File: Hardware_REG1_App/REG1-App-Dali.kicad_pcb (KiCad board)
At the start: 2 copper layers, 83 x 32.8 mm, 27 parts, among them J1 REG1_App_Connector, J3 DALI, Q1 BSS123, Q2 BC857, U1 EL357N(A)(TA)-G, U2 EL357N(A)(TA)-G, U3 STN93003, U4 STN1HNK60

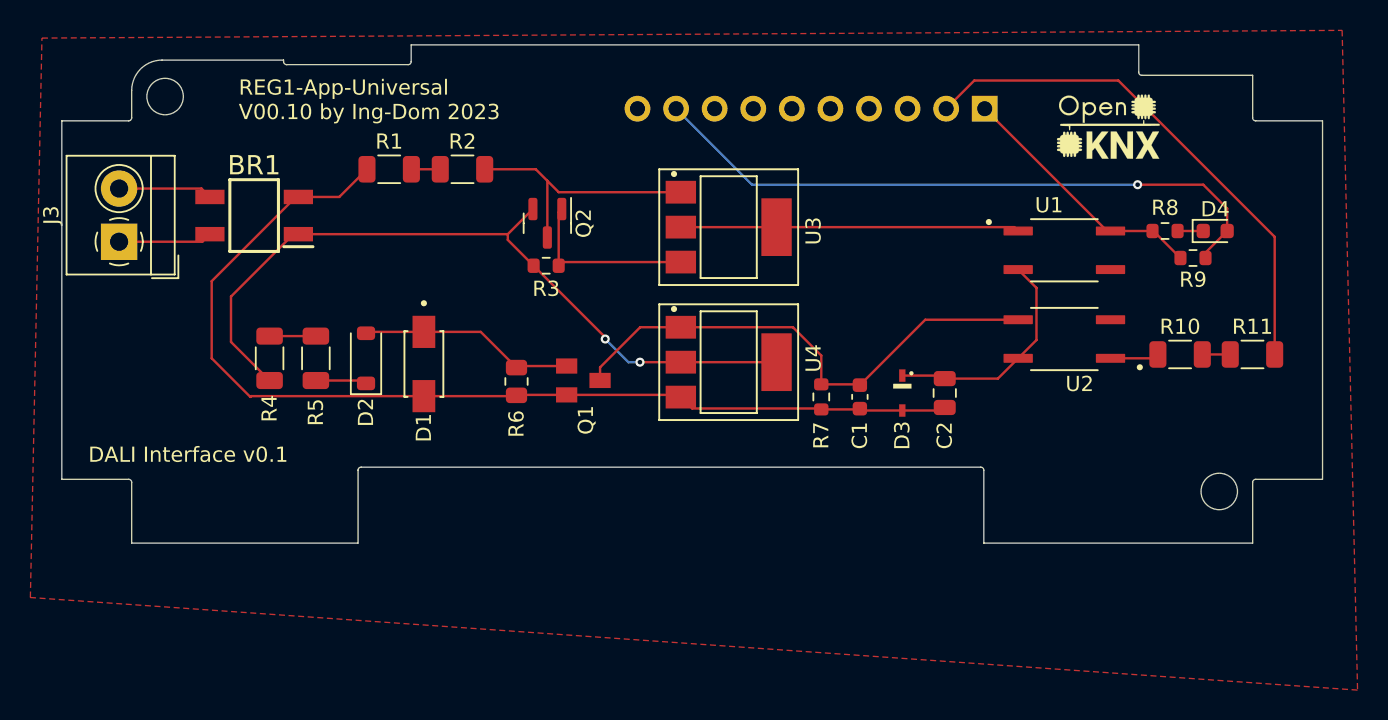
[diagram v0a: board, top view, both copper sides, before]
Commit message: updated REG1 and renamed
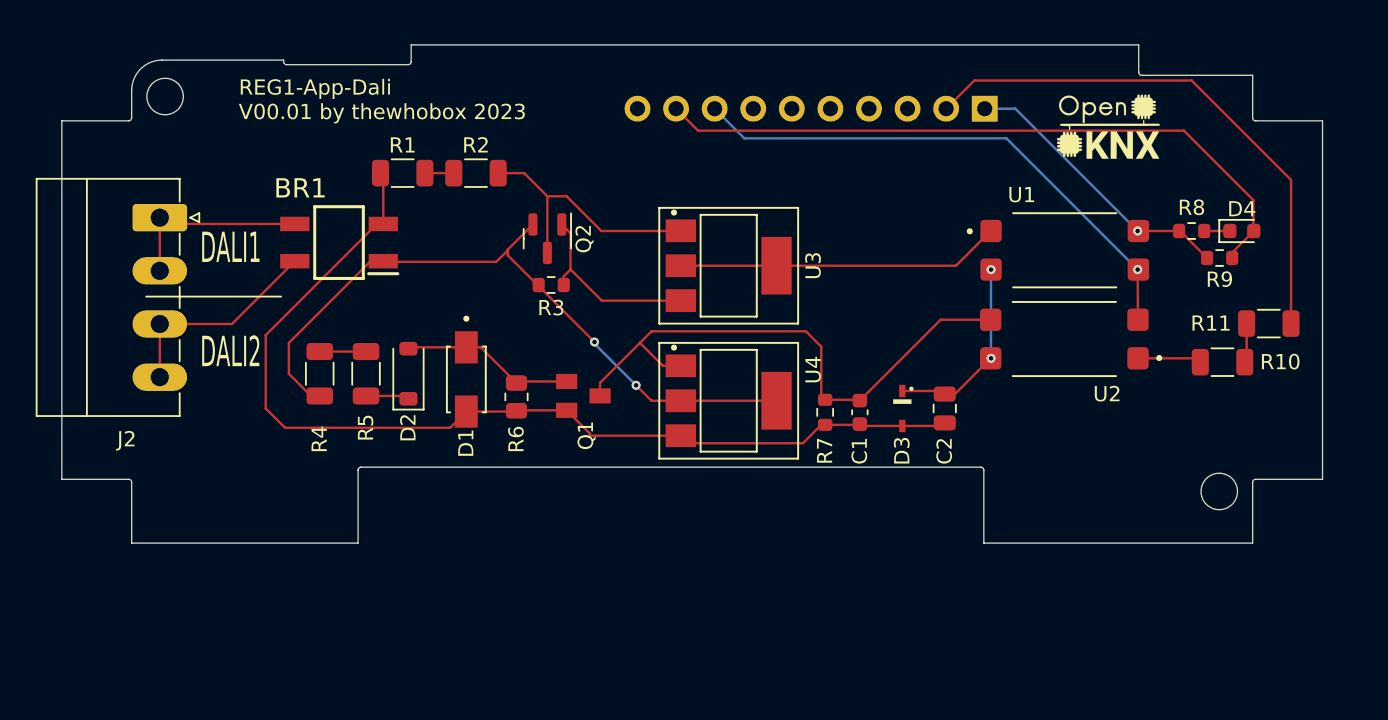
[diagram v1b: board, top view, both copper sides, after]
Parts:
- removed J3: DALI, TerminalBlock_4Ucon:TerminalBlock_4Ucon_1x02_P3.50mm_Horizontal
- added J2: Dali, Connector_Phoenix_MC:PhoenixContact_MC_1,5_4-G-3.5_1x04_P3.50mm_Horizontal, F.Cu at (76.5, 101.5)
- U1, U2: value EL357N(A)(TA)-G -> EL817S1(C)(TU)-F; footprint DALI:SOP254P700X200-4N -> DALI:SOIC254P1030X390-4N
- moved BR1 5.86 mm to (88.2, 103.1)
- moved R4 3.45 mm to (87.0, 111.8)
- moved R5 3.45 mm to (90.0, 111.8)
- moved D1 2.97 mm to (96.6, 112.1)
- moved D2 2.97 mm to (92.8, 111.8)
- moved R10 2.84 mm to (146.4, 111.0)
- moved U3 2.54 mm to (113.9, 104.6)
- moved U4 2.54 mm to (113.9, 113.5)
- moved R11 2.30 mm to (149.5, 108.4)
- moved D4 1.75 mm to (147.7, 102.4)
- moved R8 1.75 mm to (144.4, 102.4)
- moved R9 1.75 mm to (146.2, 104.1)
- moved R3 1.31 mm to (102.2, 105.9)
- moved R7 1.05 mm to (120.3, 114.3)
- moved C1 1.02 mm to (122.5, 114.3)
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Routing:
- net GND: track 0.00 -> 35.6 mm, vias 0 -> 1
- net Net-(BR1-~_2): track 6.18 -> 13.5 mm
- net Net-(BR1-~_1): track 6.21 -> 12.6 mm
- net Dali+: track 50.3 -> 45.5 mm
- net Net-(C1-Pad1): track 34.0 -> 37.4 mm
- net Net-(D2-A): track 14.3 -> 11.5 mm
- net Net-(C2-Pad1): track 15.1 -> 12.7 mm, vias 0 -> 2
- net +3.3V: track 42.8 -> 44.9 mm, vias 1 -> 0
- net DALI-: track 68.3 -> 66.5 mm
- net /D_RX: track 17.0 -> 18.7 mm, vias 0 -> 1
- net /D_TX: track 34.4 -> 35.6 mm
- net Net-(R10-Pad1): track 3.22 -> 4.21 mm
- net Net-(U1-Pad1): track 22.3 -> 21.3 mm
- net Net-(R10-Pad2): track 1.84 -> 2.59 mm
- net Net-(Q2-B): track 12.0 -> 12.5 mm
- removed copper zone on F.Cu, net GND
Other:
- board text added: "DALI1"
- board text added: "DALI2"
- board text added: "REG1-App-Dali V00.01 by thewhobox 2023"
- board text removed: "DALI Interface v0.1"
- board text removed: "REG1-App-Universal V00.10 by Ing-Dom 2023"

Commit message: updated pcb
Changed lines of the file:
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@@
     (pad "4" smd roundrect (at 4.85 -1.27 180) (size 1.41 1.47) (layers "F.Cu" "F.Paste" "F.Mask") (roundrect_rratio 0.18)
       (net 16 "/D_RX") (pintype "passive"))
+    (model "${DALI_3D}/EL817S1_C__TU_.step"
+      (offset (xyz 0 0 0))
+      (scale (xyz 1 1 1))
+      (rotate (xyz -90 0 0))
+    )
   )
   (footprint "DALI:SOT230P700X180-4N" (layer "F.Cu")
@@
     (pad "4" smd rect (at 0 -3.15 90) (size 3.8 2) (layers "F.Cu" "F.Paste" "F.Mask")
       (net 24 "Net-(U1-Pad1)") (pintype "passive"))
+    (model "${DALI_3D}/STN93003.step"
+      (offset (xyz 0 0 0))
+      (scale (xyz 1 1 1))
+      (rotate (xyz -90 0 -90))
+    )
   )
   (footprint "DALI:SOIC254P1030X390-4N" (layer "F.Cu")
@@
     (pad "4" smd roundrect (at 4.85 -1.27) (size 1.41 1.47) (layers "F.Cu" "F.Paste" "F.Mask") (roundrect_rratio 0.18)
       (net 9 "Net-(C2-Pad1)") (pintype "passive"))
+    (model "${DALI_3D}/EL817S1_C__TU_.step"
+      (offset (xyz 0 0 0))
+      (scale (xyz 1 1 1))
+      (rotate (xyz -90 0 0))
+    )
   )
   (footprint "Capacitor_SMD:C_0805_2012Metric" (layer "F.Cu")
@@
     (pad "C" smd rect (at -2.115 0 270) (size 2.12 1.5) (layers "F.Cu" "F.Paste" "F.Mask")
       (net 13 "Net-(D2-A)") (pintype "passive"))
+    (model "${DALI_3D}/1SMA4746.step"
+      (offset (xyz 0 0 0))
+      (scale (xyz 1 1 1))
+      (rotate (xyz -90 0 0))
+    )
   )
   (footprint "Resistor_SMD:R_1206_3216Metric" (layer "F.Cu")
@@
     (fp_line (start 1.6 0.8) (end -1.6 0.8)
       (stroke (width 0.1) (type solid)) (layer "F.Fab"))
-    (pad "1" smd roundrect (at -1.4625 0 90) (size 1.125 1.75) (layers "F.Cu" "F.Paste" "F.Mask") (roundrect_rratio 0.2222222222)
+    (pad "1" smd roundrect (at -1.4625 0 90) (size 1.125 1.75) (layers "F.Cu" "F.Paste" "F.Mask") (roundrect_rratio 0.222222)
       (net 21 "Net-(D2-K)") (pintype "passive"))
-    (pad "2" smd roundrect (at 1.4625 0 90) (size 1.125 1.75) (layers "F.Cu" "F.Paste" "F.Mask") (roundrect_rratio 0.2222222222)
+    (pad "2" smd roundrect (at 1.4625 0 90) (size 1.125 1.75) (layers "F.Cu" "F.Paste" "F.Mask") (roundrect_rratio 0.222222)
       (net 20 "Net-(R4-Pad1)") (pintype "passive"))
     (model "${KICAD6_3DMODEL_DIR}/Resistor_SMD.3dshapes/R_1206_3216Metric.wrl"
@@
     (fp_line (start 1.6 0.8) (end -1.6 0.8)
       (stroke (width 0.1) (type solid)) (layer "F.Fab"))
-    (pad "1" smd roundrect (at -1.4625 0) (size 1.125 1.75) (layers "F.Cu" "F.Paste" "F.Mask") (roundrect_rratio 0.2222222222)
+    (pad "1" smd roundrect (at -1.4625 0) (size 1.125 1.75) (layers "F.Cu" "F.Paste" "F.Mask") (roundrect_rratio 0.222222)
       (net 23 "Net-(R10-Pad2)") (pintype "passive"))
-    (pad "2" smd roundrect (at 1.4625 0) (size 1.125 1.75) (layers "F.Cu" "F.Paste" "F.Mask") (roundrect_rratio 0.2222222222)
+    (pad "2" smd roundrect (at 1.4625 0) (size 1.125 1.75) (layers "F.Cu" "F.Paste" "F.Mask") (roundrect_rratio 0.222222)
       (net 17 "/D_TX") (pintype "passive"))
     (model "${KICAD6_3DMODEL_DIR}/Resistor_SMD.3dshapes/R_1206_3216Metric.wrl"
@@
     (fp_line (start 1.6 0.8) (end -1.6 0.8)
       (stroke (width 0.1) (type solid)) (layer "F.Fab"))
-    (pad "1" smd roundrect (at -1.4625 0 270) (size 1.125 1.75) (layers "F.Cu" "F.Paste" "F.Mask") (roundrect_rratio 0.2222222222)
+    (pad "1" smd roundrect (at -1.4625 0 270) (size 1.125 1.75) (layers "F.Cu" "F.Paste" "F.Mask") (roundrect_rratio 0.222222)
       (net 20 "Net-(R4-Pad1)") (pintype "passive"))
-    (pad "2" smd roundrect (at 1.4625 0 270) (size 1.125 1.75) (layers "F.Cu" "F.Paste" "F.Mask") (roundrect_rratio 0.2222222222)
+    (pad "2" smd roundrect (at 1.4625 0 270) (size 1.125 1.75) (layers "F.Cu" "F.Paste" "F.Mask") (roundrect_rratio 0.222222)
       (net 1 "Dali+") (pintype "passive"))
     (model "${KICAD6_3DMODEL_DIR}/Resistor_SMD.3dshapes/R_1206_3216Metric.wrl"
@@
     (fp_line (start 1.6 0.8) (end -1.6 0.8)
       (stroke (width 0.1) (type solid)) (layer "F.Fab"))
-    (pad "1" smd roundrect (at -1.4625 0) (size 1.125 1.75) (layers "F.Cu" "F.Paste" "F.Mask") (roundrect_rratio 0.2222222222)
+    (pad "1" smd roundrect (at -1.4625 0) (size 1.125 1.75) (layers "F.Cu" "F.Paste" "F.Mask") (roundrect_rratio 0.222222)
       (net 22 "Net-(R10-Pad1)") (pintype "passive"))
-    (pad "2" smd roundrect (at 1.4625 0) (size 1.125 1.75) (layers "F.Cu" "F.Paste" "F.Mask") (roundrect_rratio 0.2222222222)
+    (pad "2" smd roundrect (at 1.4625 0) (size 1.125 1.75) (layers "F.Cu" "F.Paste" "F.Mask") (roundrect_rratio 0.222222)
       (net 23 "Net-(R10-Pad2)") (pintype "passive"))
     (model "${KICAD6_3DMODEL_DIR}/Resistor_SMD.3dshapes/R_1206_3216Metric.wrl"
@@
     (fp_line (start 1.6 0.8) (end -1.6 0.8)
       (stroke (width 0.1) (type solid)) (layer "F.Fab"))
-    (pad "1" smd roundrect (at -1.4625 0) (size 1.125 1.75) (layers "F.Cu" "F.Paste" "F.Mask") (roundrect_rratio 0.2222222222)
+    (pad "1" smd roundrect (at -1.4625 0) (size 1.125 1.75) (layers "F.Cu" "F.Paste" "F.Mask") (roundrect_rratio 0.222222)
       (net 19 "Net-(R1-Pad2)") (pintype "passive"))
-    (pad "2" smd roundrect (at 1.4625 0) (size 1.125 1.75) (layers "F.Cu" "F.Paste" "F.Mask") (roundrect_rratio 0.2222222222)
+    (pad "2" smd roundrect (at 1.4625 0) (size 1.125 1.75) (layers "F.Cu" "F.Paste" "F.Mask") (roundrect_rratio 0.222222)
       (net 26 "Net-(Q2-C)") (pintype "passive"))
     (model "${KICAD6_3DMODEL_DIR}/Resistor_SMD.3dshapes/R_1206_3216Metric.wrl"
@@
     (fp_line (start 1.6 0.8) (end -1.6 0.8)
       (stroke (width 0.1) (type solid)) (layer "F.Fab"))
-    (pad "1" smd roundrect (at -1.4625 0) (size 1.125 1.75) (layers "F.Cu" "F.Paste" "F.Mask") (roundrect_rratio 0.2222222222)
+    (pad "1" smd roundrect (at -1.4625 0) (size 1.125 1.75) (layers "F.Cu" "F.Paste" "F.Mask") (roundrect_rratio 0.222222)
       (net 2 "DALI-") (pintype "passive"))
-    (pad "2" smd roundrect (at 1.4625 0) (size 1.125 1.75) (layers "F.Cu" "F.Paste" "F.Mask") (roundrect_rratio 0.2222222222)
+    (pad "2" smd roundrect (at 1.4625 0) (size 1.125 1.75) (layers "F.Cu" "F.Paste" "F.Mask") (roundrect_rratio 0.222222)
       (net 19 "Net-(R1-Pad2)") (pintype "passive"))
     (model "${KICAD6_3DMODEL_DIR}/Resistor_SMD.3dshapes/R_1206_3216Metric.wrl"
@@
     (pad "4" smd rect (at 2.912 -1.225 270) (size 0.95 1.925) (layers "F.Cu" "F.Paste" "F.Mask")
       (net 12 "Net-(BR1-~_2)") (pinfunction "~_2") (pintype "passive"))
-    (model "MB10S.stp"
+    (model "${DALI_3D}/MB10S.stp"
       (offset (xyz 0 0 0))
       (scale (xyz 1 1 1))
@@
     (fp_line (start 1 0.625) (end -1 0.625)
       (stroke (width 0.1) (type solid)) (layer "F.Fab"))
-    (pad "1" smd roundrect (at -0.9125 0 90) (size 1.025 1.4) (layers "F.Cu" "F.Paste" "F.Mask") (roundrect_rratio 0.243902439)
+    (pad "1" smd roundrect (at -0.9125 0 90) (size 1.025 1.4) (layers "F.Cu" "F.Paste" "F.Mask") (roundrect_rratio 0.243902)
       (net 2 "DALI-") (pintype "passive"))
-    (pad "2" smd roundrect (at 0.9125 0 90) (size 1.025 1.4) (layers "F.Cu" "F.Paste" "F.Mask") (roundrect_rratio 0.243902439)
+    (pad "2" smd roundrect (at 0.9125 0 90) (size 1.025 1.4) (layers "F.Cu" "F.Paste" "F.Mask") (roundrect_rratio 0.243902)
       (net 13 "Net-(D2-A)") (pintype "passive"))
     (model "${KICAD6_3DMODEL_DIR}/Resistor_SMD.3dshapes/R_0805_2012Metric.wrl"
@@
     (fp_line (start 12.95 8) (end 12.95 -1.2)
       (stroke (width 0.1) (type solid)) (layer "F.Fab"))
-    (pad "1" thru_hole roundrect (at 0 0 270) (size 1.8 3.6) (drill 1.2) (layers "*.Cu" "*.Mask") (roundrect_rratio 0.1388888889)
+    (pad "1" thru_hole roundrect (at 0 0 270) (size 1.8 3.6) (drill 1.2) (layers "*.Cu" "*.Mask") (roundrect_rratio 0.138889)
       (net 11 "Net-(BR1-~_1)") (pinfunction "Pin_1") (pintype "passive"))
     (pad "2" thru_hole oval (at 3.5 0 270) (size 1.8 3.6) (drill 1.2) (layers "*.Cu" "*.Mask")
@@
     (pad "4" smd rect (at 0 -3.15 90) (size 3.8 2) (layers "F.Cu" "F.Paste" "F.Mask")
       (net 1 "Dali+") (pintype "passive"))
+    (model "${DALI_3D}/STN1HNK60.step"
+      (offset (xyz 0 0 0))
+      (scale (xyz 1 1 1))
+      (rotate (xyz -90 0 -90))
+    )
   )
   (footprint "Connector_PinHeader_2.54mm:PinHeader_1x10_P2.54mm_Horizontal" locked (layer "B.Cu")
@@
     (pad "10" thru_hole oval locked (at 0 -22.86 90) (size 1.7 1.7) (drill 1) (layers "*.Cu" "*.Mask")
       (net 10 "unconnected-(J1-VCC2-Pad10)") (pinfunction "VCC2") (pintype "power_out"))
-    (model "${KISYS3DMOD}/Connector_PinHeader_2.54mm.3dshapes/PinHeader_1x10_P2.54mm_Horizontal.wrl"
-      (offset (xyz 0 0 0))
-      (scale (xyz 1 1 1))
+    (model "${KICAD6_3DMODEL_DIR}/Connector_PinHeader_2.54mm.3dshapes/PinHeader_1x10_P2.54mm_Horizontal.wrl"
+      (offset (xyz 0 0 0))
+      (scale (xyz 1 1 1))
